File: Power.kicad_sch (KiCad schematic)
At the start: 0 parts

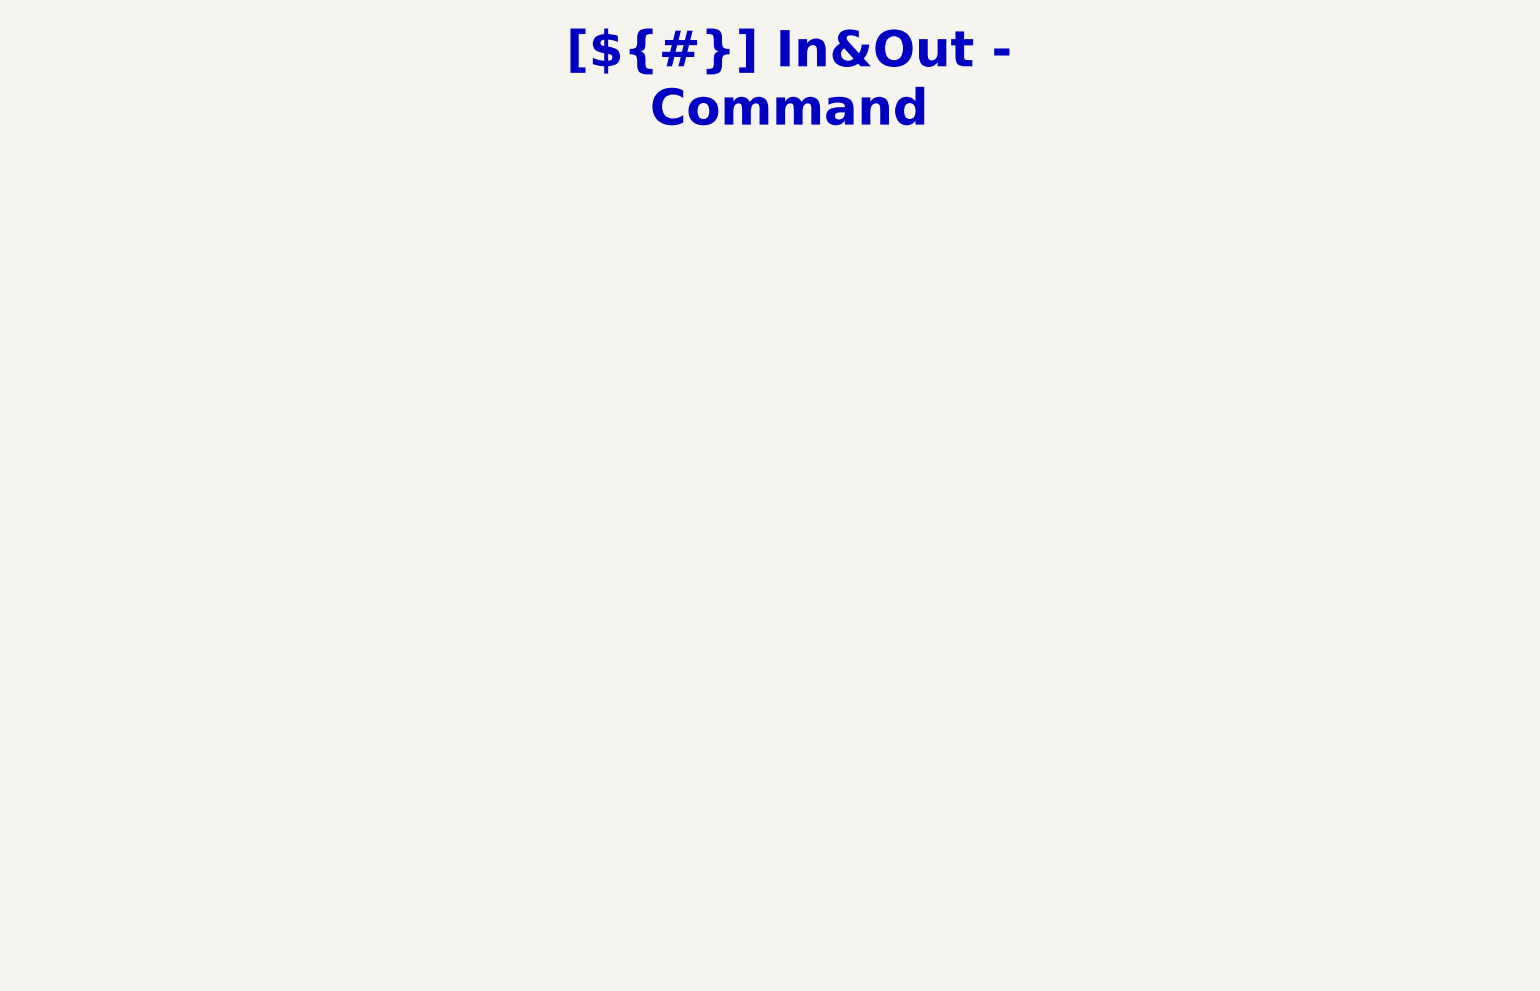
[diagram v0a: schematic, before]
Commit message: [Schematic][Added] Power Supply, SMPS(5V) & LDO(3V3)
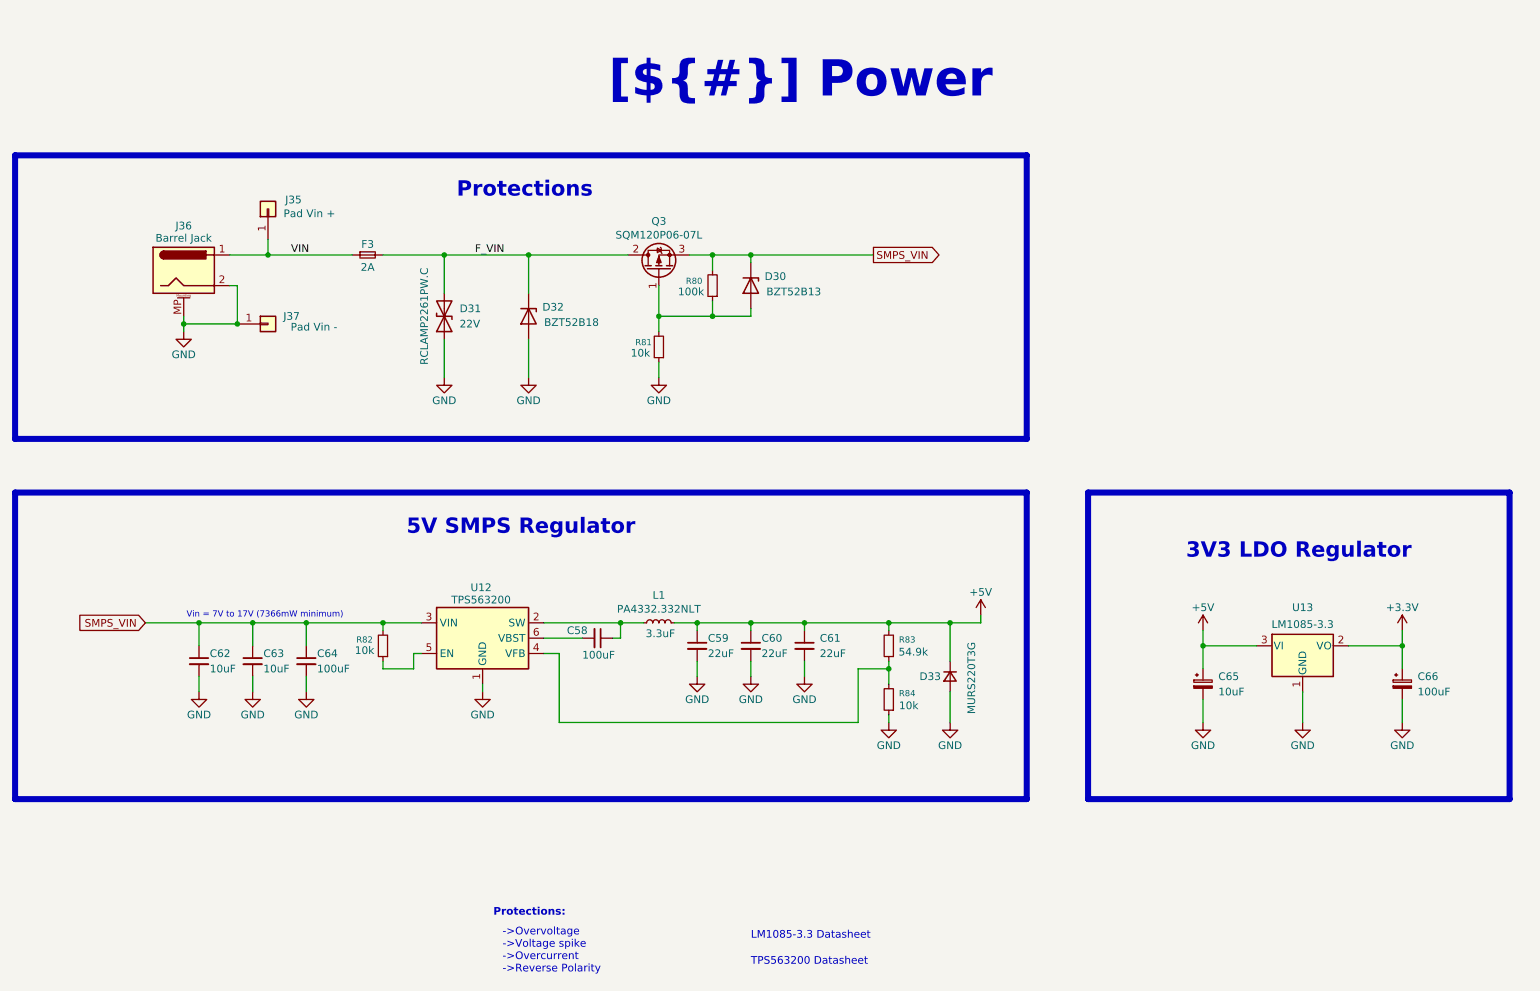
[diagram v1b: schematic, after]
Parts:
- added C58, C64: 100uF, Capacitor_SMD:C_0805_2012Metric_Pad1.18x1.45mm_HandSolder, symbol Device:C_Small
- added C59, C60, C61: 22uF, Capacitor_SMD:C_0805_2012Metric_Pad1.18x1.45mm_HandSolder, symbol Device:C_Small
- added C62, C63: 10uF, Capacitor_SMD:C_0805_2012Metric_Pad1.18x1.45mm_HandSolder, symbol Device:C_Small
- added C65: 10uF, Capacitor_SMD:CP_Elec_5x5.3, symbol Device:C_Polarized_Small
- added C66: 100uF, Capacitor_Tantalum_SMD:CP_EIA-7343-15_Kemet-W_HandSolder, symbol Device:C_Polarized_Small
- added D30: 13V, Diode_SMD:D_SOD-123F, symbol Diode:BZT52Bxx
- added D31: 22V, Diode_SMD:D_0603_1608Metric_Pad1.05x0.95mm_HandSolder, symbol Device:D_TVS
- added D32: 18V, Diode_SMD:D_SOD-123F, symbol Diode:BZT52Bxx
- added D33: 2A, Diode_SMD:D_SMB, symbol Device:D_Small
- added F3: 2A, Fuse:Fuse_2920_7451Metric_Pad2.10x5.45mm_HandSolder, symbol Device:Fuse_Small
- added J35, J37: *, Connector_Wire:SolderWirePad_1x01_SMD_4x8mm, symbol Connector_Generic:Conn_01x01
- added J36: *, Connector_BarrelJack:BarrelJack_Horizontal, symbol Connector:Barrel_Jack_MountingPin
- added L1: 3.3uF, PCM_SparkFun-Coil:Inductor_4.7x4.7mm, symbol PCM_SparkFun-Coil:10uH_5x5mm_1.0A
- added Q3: *, Package_TO_SOT_SMD:TO-263-3_TabPin2, symbol PCM_SparkFun-DiscreteSemi:Q_PMOS_GDS
- added R80: 100k, Resistor_SMD:R_0805_2012Metric_Pad1.20x1.40mm_HandSolder, symbol Device:R_Small
- added R81, R82, R84: 10k, Resistor_SMD:R_0805_2012Metric_Pad1.20x1.40mm_HandSolder, symbol Device:R_Small
- added R83: 54.9k, Resistor_SMD:R_0805_2012Metric_Pad1.20x1.40mm_HandSolder, symbol Device:R_Small
- added U12: 5V, Package_TO_SOT_SMD:SOT-23-6, symbol Regulator_Switching:TPS563200
- added U13: 3V3, Package_TO_SOT_SMD:TO-263-3_TabPin2, symbol Regulator_Linear:LM1085-3.3
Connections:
- new net: D30.2 (A), Q3.1 (G), R80.1, R81.2
- new net: C58.1, L1.1, U12.2 (SW)
- new net: C58.2, U12.6 (VBST)
- new net: R83.1, R84.2, U12.4 (VFB)
- new net: R82.1, U12.5 (EN)
- new net +3.3V: C66.1, U13.2 (VO)
- new net +5V: C59.1, C60.1, C61.1, C65.1, D33.1 (K), L1.2, R83.2, U13.3 (VI)
- new net F_VIN: D31.2 (A2), D32.1 (K), F3.2, Q3.2 (D)
- new net GND: C59.2, C60.2, C61.2, C62.2, C63.2, C64.2, C65.2, C66.2, D31.1 (A1), D32.2 (A), D33.2 (A), J36.2, J36.MP (MountPin), J37.1 (Pin_1), R81.1, R84.1, U12.1 (GND), U13.1 (GND)
- new net SMPS_VIN: C62.1, C63.1, C64.1, D30.1 (K), Q3.3 (S), R80.2, R82.2, U12.3 (VIN)
- new net VIN: F3.1, J35.1 (Pin_1), J36.1
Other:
- note added: "->Overvoltage ->Voltage spike ->Overcurrent ->Reverse Polarity"
- note added: "LM1085-3.3 Datasheet"
- note added: "Protections:"
- note added: "TPS563200 Datasheet"
- note added: "Vin = 7V to 17V (7366mW minimum)"
- title: In&Out - Command -> Power

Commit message: [Project][Added] CI/CD environment
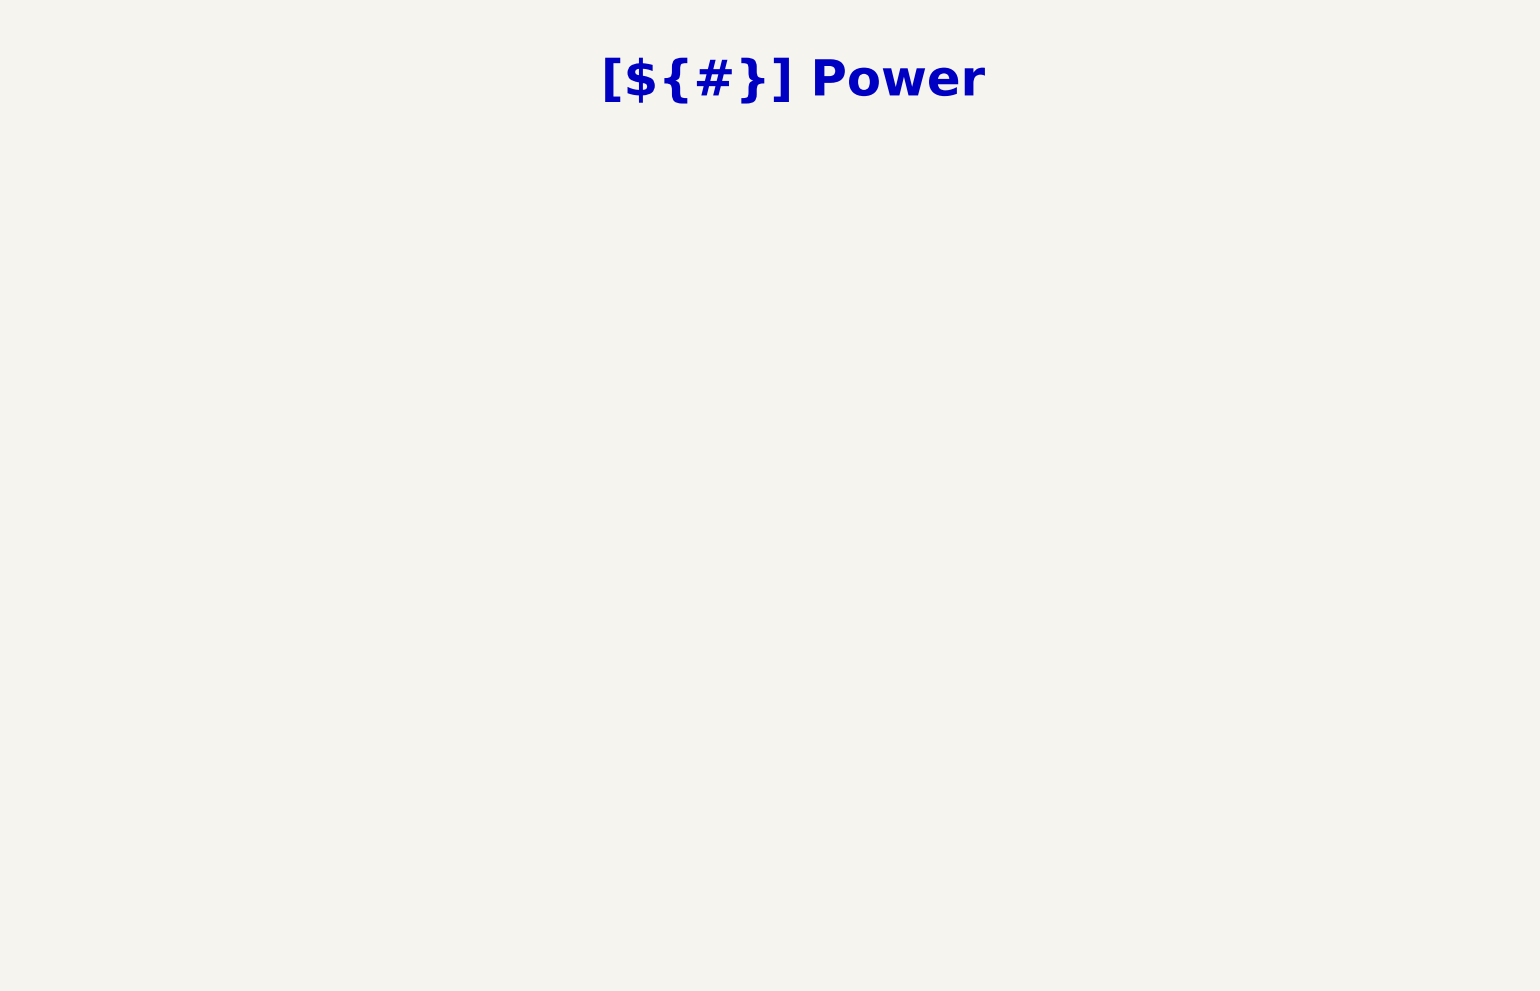
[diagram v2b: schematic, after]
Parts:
- removed C58, C64: 100uF, Capacitor_SMD:C_0805_2012Metric_Pad1.18x1.45mm_HandSolder, symbol Device:C_Small
- removed C59, C60, C61: 22uF, Capacitor_SMD:C_0805_2012Metric_Pad1.18x1.45mm_HandSolder, symbol Device:C_Small
- removed C62, C63: 10uF, Capacitor_SMD:C_0805_2012Metric_Pad1.18x1.45mm_HandSolder, symbol Device:C_Small
- removed C65: 10uF, Capacitor_SMD:CP_Elec_5x5.3, symbol Device:C_Polarized_Small
- removed C66: 100uF, Capacitor_Tantalum_SMD:CP_EIA-7343-15_Kemet-W_HandSolder, symbol Device:C_Polarized_Small
- removed D30: 13V, Diode_SMD:D_SOD-123F, symbol Diode:BZT52Bxx
- removed D31: 22V, Diode_SMD:D_0603_1608Metric_Pad1.05x0.95mm_HandSolder, symbol Device:D_TVS
- removed D32: 18V, Diode_SMD:D_SOD-123F, symbol Diode:BZT52Bxx
- removed D33: 2A, Diode_SMD:D_SMB, symbol Device:D_Small
- removed F3: 2A, Fuse:Fuse_2920_7451Metric_Pad2.10x5.45mm_HandSolder, symbol Device:Fuse_Small
- removed J35, J37: *, Connector_Wire:SolderWirePad_1x01_SMD_4x8mm, symbol Connector_Generic:Conn_01x01
- removed J36: *, Connector_BarrelJack:BarrelJack_Horizontal, symbol Connector:Barrel_Jack_MountingPin
- removed L1: 3.3uF, PCM_SparkFun-Coil:Inductor_4.7x4.7mm, symbol PCM_SparkFun-Coil:10uH_5x5mm_1.0A
- removed Q3: *, Package_TO_SOT_SMD:TO-263-3_TabPin2, symbol PCM_SparkFun-DiscreteSemi:Q_PMOS_GDS
- removed R80: 100k, Resistor_SMD:R_0805_2012Metric_Pad1.20x1.40mm_HandSolder, symbol Device:R_Small
- removed R81, R82, R84: 10k, Resistor_SMD:R_0805_2012Metric_Pad1.20x1.40mm_HandSolder, symbol Device:R_Small
- removed R83: 54.9k, Resistor_SMD:R_0805_2012Metric_Pad1.20x1.40mm_HandSolder, symbol Device:R_Small
- removed U12: 5V, Package_TO_SOT_SMD:SOT-23-6, symbol Regulator_Switching:TPS563200
- removed U13: 3V3, Package_TO_SOT_SMD:TO-263-3_TabPin2, symbol Regulator_Linear:LM1085-3.3
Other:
- note removed: "->Overvoltage ->Voltage spike ->Overcurrent ->Reverse Polarity"
- note removed: "LM1085-3.3 Datasheet"
- note removed: "Protections:"
- note removed: "TPS563200 Datasheet"
- note removed: "Vin = 7V to 17V (7366mW minimum)"

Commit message: [Schematic][Added] Power Supply, SMPS(5V) & LDO(3V3)
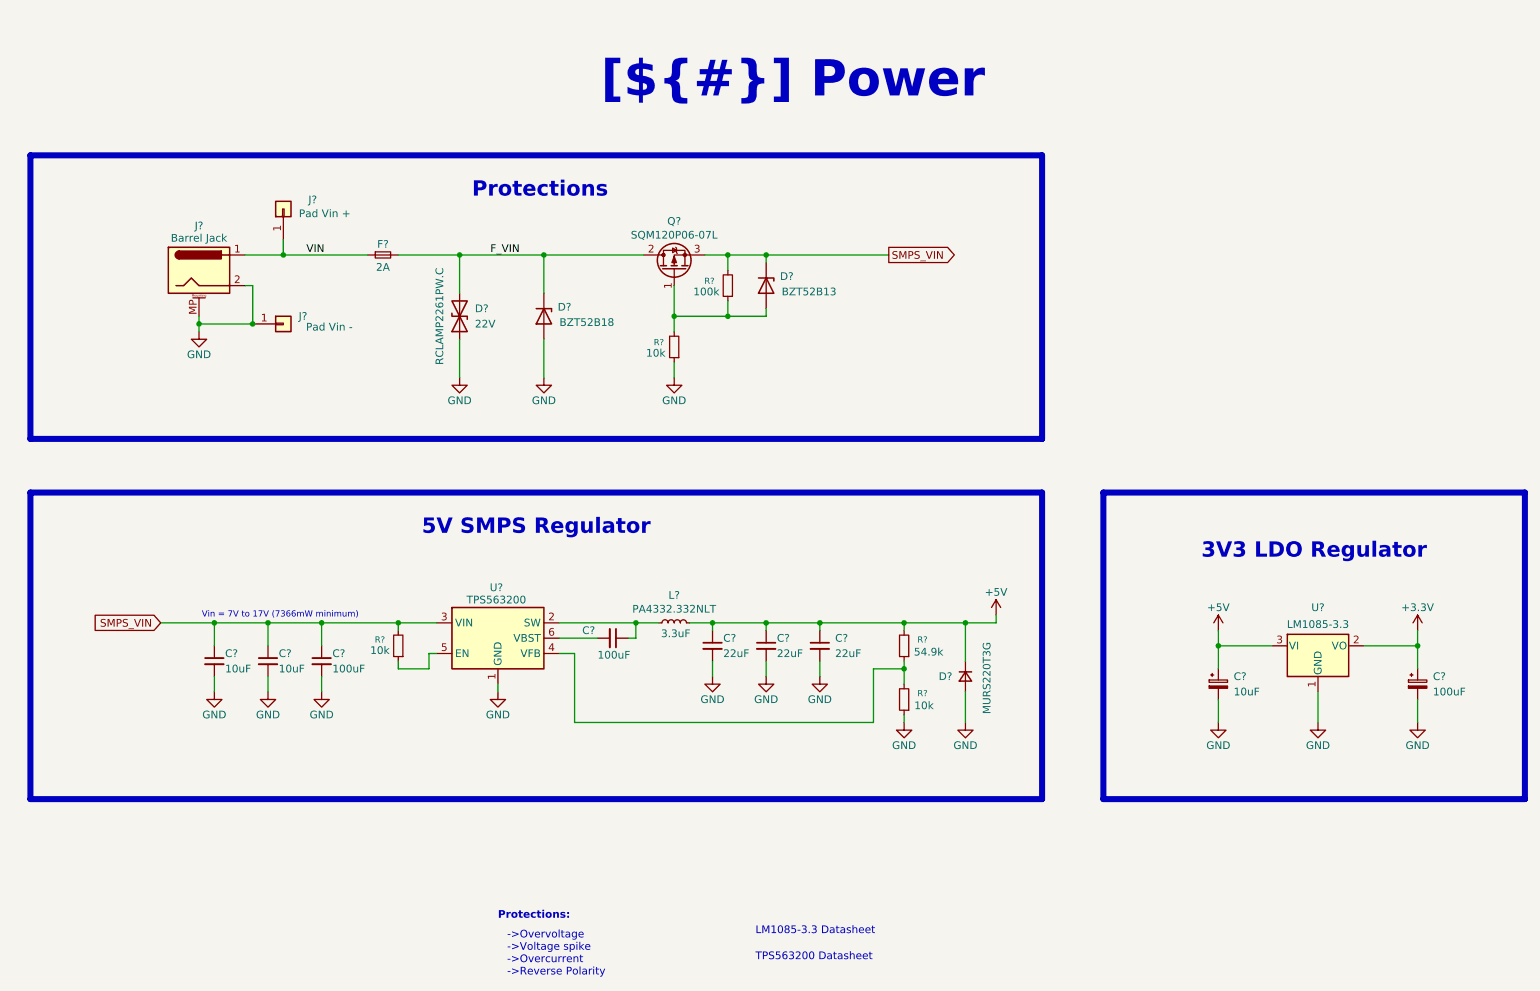
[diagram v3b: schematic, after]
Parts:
- added C? (x2): 100uF, Capacitor_SMD:C_0805_2012Metric_Pad1.18x1.45mm_HandSolder, symbol Device:C_Small
- added C? (x3): 22uF, Capacitor_SMD:C_0805_2012Metric_Pad1.18x1.45mm_HandSolder, symbol Device:C_Small
- added C?: 10uF, Capacitor_SMD:CP_Elec_5x5.3, symbol Device:C_Polarized_Small
- added C?: 100uF, Capacitor_Tantalum_SMD:CP_EIA-7343-15_Kemet-W_HandSolder, symbol Device:C_Polarized_Small
- added C? (x2): 10uF, Capacitor_SMD:C_0805_2012Metric_Pad1.18x1.45mm_HandSolder, symbol Device:C_Small
- added D?: 13V, Diode_SMD:D_SOD-123F, symbol Diode:BZT52Bxx
- added D?: 2A, Diode_SMD:D_SMB, symbol Device:D_Small
- added D?: 18V, Diode_SMD:D_SOD-123F, symbol Diode:BZT52Bxx
- added D?: 22V, Diode_SMD:D_0603_1608Metric_Pad1.05x0.95mm_HandSolder, symbol Device:D_TVS
- added F?: 2A, Fuse:Fuse_2920_7451Metric_Pad2.10x5.45mm_HandSolder, symbol Device:Fuse_Small
- added J? (x2): *, Connector_Wire:SolderWirePad_1x01_SMD_4x8mm, symbol Connector_Generic:Conn_01x01
- added J?: *, Connector_BarrelJack:BarrelJack_Horizontal, symbol Connector:Barrel_Jack_MountingPin
- added L?: 3.3uF, PCM_SparkFun-Coil:Inductor_4.7x4.7mm, symbol PCM_SparkFun-Coil:10uH_5x5mm_1.0A
- added Q?: *, Package_TO_SOT_SMD:TO-263-3_TabPin2, symbol PCM_SparkFun-DiscreteSemi:Q_PMOS_GDS
- added R?: 100k, Resistor_SMD:R_0805_2012Metric_Pad1.20x1.40mm_HandSolder, symbol Device:R_Small
- added R?: 54.9k, Resistor_SMD:R_0805_2012Metric_Pad1.20x1.40mm_HandSolder, symbol Device:R_Small
- added R? (x3): 10k, Resistor_SMD:R_0805_2012Metric_Pad1.20x1.40mm_HandSolder, symbol Device:R_Small
- added U?: 3V3, Package_TO_SOT_SMD:TO-263-3_TabPin2, symbol Regulator_Linear:LM1085-3.3
- added U?: 5V, Package_TO_SOT_SMD:SOT-23-6, symbol Regulator_Switching:TPS563200
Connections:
- new net: D?.2 (A), Q?.1 (G), R?.1, R?.2
- new net: C?.1, L?.1, U?.2 (SW)
- new net: C?.2, U?.6 (VBST)
- new net: R?.1, R?.2, U?.4 (VFB)
- new net: R?.1, U?.5 (EN)
- new net +3.3V: C?.1, U?.2 (VO)
- new net +5V: C?.1, C?.1, C?.1, C?.1, D?.1 (K), L?.2, R?.2, U?.3 (VI)
- new net F_VIN: D?.1 (K), D?.2 (A2), F?.2, Q?.2 (D)
- new net GND: C?.2, C?.2, C?.2, C?.2, C?.2, C?.2, C?.2, C?.2, D?.1 (A1), D?.2 (A), D?.2 (A), J?.1 (Pin_1), J?.2, J?.MP (MountPin), R?.1, R?.1, U?.1 (GND), U?.1 (GND)
- new net SMPS_VIN: C?.1, C?.1, C?.1, D?.1 (K), Q?.3 (S), R?.2, R?.2, U?.3 (VIN)
- new net VIN: F?.1, J?.1, J?.1 (Pin_1)
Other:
- note added: "->Overvoltage ->Voltage spike ->Overcurrent ->Reverse Polarity"
- note added: "LM1085-3.3 Datasheet"
- note added: "Protections:"
- note added: "TPS563200 Datasheet"
- note added: "Vin = 7V to 17V (7366mW minimum)"

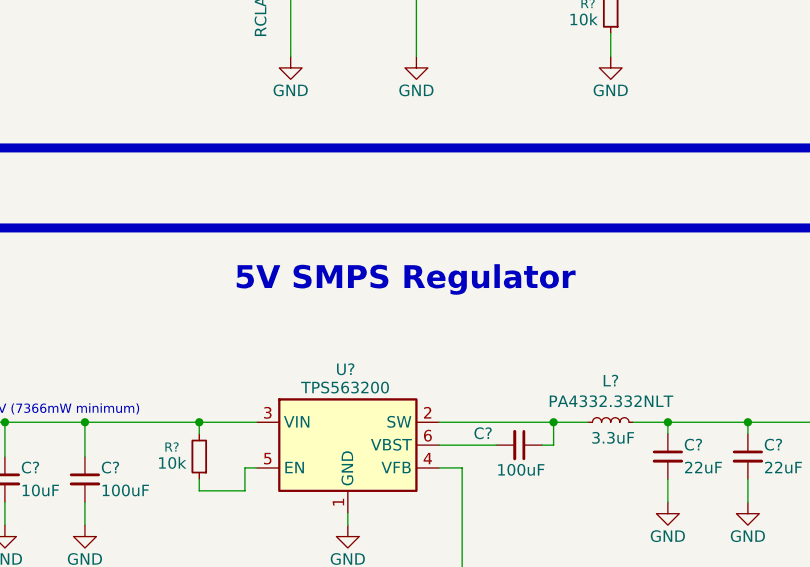
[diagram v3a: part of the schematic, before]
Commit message: [Schematic][Add] Add of a new page : MCU Expander
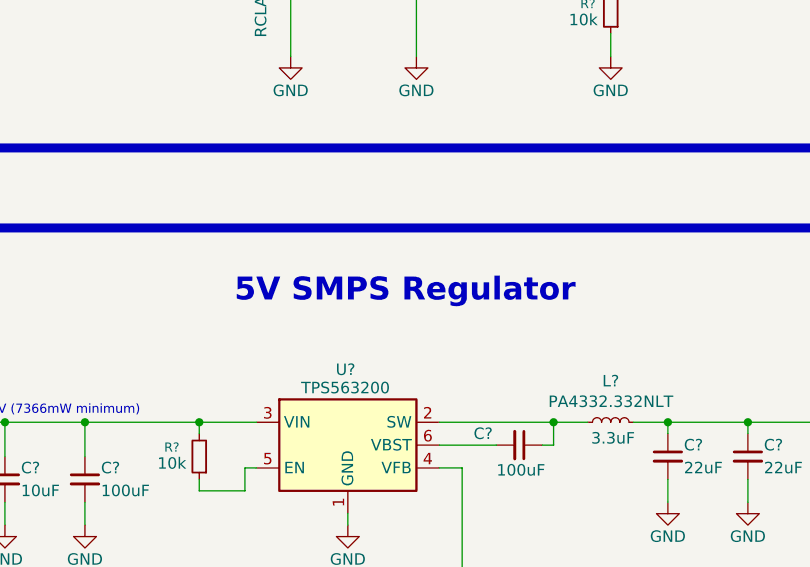
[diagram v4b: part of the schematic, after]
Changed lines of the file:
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@@
 	(text_box "5V SMPS Regulator"
 		(exclude_from_sim no)
-		(at 25.4 91.2997 0)
+		(at 25.4 92.5697 0)
 		(size 165.1 7.7603)
 		(margins 1.9049 1.9049 1.9049 1.9049)

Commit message: [Schematic][Modify] Annotation of all  the components
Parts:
- gave numbers to parts that had none: 26

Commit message: [Schematic][Modify] Annotation of all  the components
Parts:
- renumbered C60 to C57, C61 to C58, C62 to C59, C63 to C60, C57 to C61, C58 to C62, C59 to C63, D32 to D30, D30 to D31, D31 to D32, J35 to J34, J34 to J35, R82 to R80, R80 to R82
